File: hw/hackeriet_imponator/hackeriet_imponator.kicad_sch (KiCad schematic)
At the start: 35 parts, among them J1 USB4085-GF-A, J2 UPDI programming, J3 External Battery Connector, J4 Shitty Add On, J5 Unused pins, SW1 SW_SPDT, SW2 User configurable, SW3 User configurable, U1 ATtiny804-SS, U2 MCP2221AxSL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

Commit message: More routing
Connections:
- net ACC_ENABLE: now also U1.2 (PA4); no longer U1.4 (PA6)
- net ACC_INT: now also U1.13 (PA3); no longer U1.3 (PA5)
- net at SW3.1: now also U1.4 (PA6); no longer U1.2 (PA4)
- net at SW2.1: now also U1.3 (PA5); no longer U1.13 (PA3)
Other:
- moved on the sheet: SW2, SW3
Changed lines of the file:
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@@
 	(wire
 		(pts
-			(xy 81.28 58.42) (xy 109.22 58.42)
+			(xy 40.64 48.26) (xy 50.8 48.26)
 		)
 		(stroke
@@
 	(wire
 		(pts
-			(xy 40.64 48.26) (xy 50.8 48.26)
+			(xy 187.96 139.7) (xy 187.96 137.16)
 		)
 		(stroke
@@
 	(wire
 		(pts
-			(xy 187.96 139.7) (xy 187.96 137.16)
+			(xy 111.76 66.04) (xy 111.76 63.5)
 		)
 		(stroke
@@
 	(wire
 		(pts
-			(xy 111.76 55.88) (xy 111.76 59.69)
+			(xy 81.28 63.5) (xy 111.76 63.5)
 		)
 		(stroke
@@
 	(wire
 		(pts
-			(xy 121.92 64.77) (xy 124.46 64.77)
+			(xy 121.92 66.04) (xy 124.46 66.04)
 		)
 		(stroke
@@
 	(wire
 		(pts
-			(xy 109.22 58.42) (xy 109.22 64.77)
+			(xy 168.91 90.17) (xy 179.07 90.17)
 		)
 		(stroke
@@
 	(wire
 		(pts
-			(xy 168.91 90.17) (xy 179.07 90.17)
+			(xy 69.85 118.11) (xy 72.39 118.11)
 		)
 		(stroke
@@
 	(wire
 		(pts
-			(xy 69.85 118.11) (xy 72.39 118.11)
+			(xy 81.28 60.96) (xy 111.76 60.96)
 		)
 		(stroke
@@
 	(wire
 		(pts
-			(xy 121.92 59.69) (xy 124.46 59.69)
+			(xy 121.92 60.96) (xy 124.46 60.96)
 		)
 		(stroke
@@
 	(wire
 		(pts
-			(xy 81.28 55.88) (xy 111.76 55.88)
-		)
-		(stroke
-			(width 0)
-			(type default)
-		)
-	)
-	(wire
-		(pts
 			(xy 62.23 114.3) (xy 62.23 113.03)
 		)
@@
 	(wire
 		(pts
-			(xy 109.22 64.77) (xy 111.76 64.77)
-		)
-		(stroke
-			(width 0)
-			(type default)
-		)
-	)
-	(wire
-		(pts
 			(xy 96.52 179.07) (xy 99.06 179.07)
 		)
@@
 		)
 	)
-	(global_label "PA5"
-		(shape input)
-		(at 81.28 60.96 0)
-		(fields_autoplaced yes)
-		(effects
-			(font
-				(size 1.27 1.27)
-			)
-			(justify left)
-		)
-		(property "Intersheetrefs" "${INTERSHEET_REFS}"
-			(at 87.8333 60.96 0)
-			(effects
-				(font
-					(size 1.27 1.27)
-				)
-				(justify left)
-				(hide yes)
-			)
-		)
-	)
 	(global_label "WS2812B LED RGB Control logo"
 		(shape input)
@@
 		)
 	)
-	(global_label "PA5"
+	(global_label "PA3"
 		(shape input)
 		(at 168.91 92.71 180)
@@
 		)
 	)
-	(global_label "PA5"
+	(global_label "PA3"
 		(shape input)
 		(at 130.81 180.34 180)
@@
 		)
 	)
-	(global_label "PA6"
+	(global_label "PA4"
 		(shape input)
 		(at 130.81 182.88 180)
@@
 		)
 	)
-	(global_label "SDA"
+	(global_label "PA4"
 		(shape input)
-		(at 111.76 179.07 0)
+		(at 81.28 58.42 0)
 		(fields_autoplaced yes)
 		(effects
@@
 		)
 		(property "Intersheetrefs" "${INTERSHEET_REFS}"
-			(at 118.3133 179.07 0)
+			(at 87.8333 58.42 0)
 			(effects
 				(font
@@
 		)
 	)
-	(global_label "D-"
+	(global_label "SDA"
 		(shape input)
-		(at 78.74 128.27 180)
+		(at 111.76 179.07 0)
 		(fields_autoplaced yes)
 		(effects
@@
 				(size 1.27 1.27)
 			)
-			(justify right)
+			(justify left)
 		)
 		(property "Intersheetrefs" "${INTERSHEET_REFS}"
-			(at 72.9124 128.27 0)
+			(at 118.3133 179.07 0)
 			(effects
 				(font
 					(size 1.27 1.27)
 				)
-				(justify right)
+				(justify left)
 				(hide yes)
 			)
 		)
 	)
-	(global_label "PA6"
+	(global_label "D-"
 		(shape input)
-		(at 81.28 63.5 0)
+		(at 78.74 128.27 180)
 		(fields_autoplaced yes)
 		(effects
@@
 				(size 1.27 1.27)
 			)
-			(justify left)
+			(justify right)
 		)
 		(property "Intersheetrefs" "${INTERSHEET_REFS}"
-			(at 87.8333 63.5 0)
+			(at 72.9124 128.27 0)
 			(effects
 				(font
 					(size 1.27 1.27)
 				)
-				(justify left)
+				(justify right)
 				(hide yes)
 			)
@@
 		)
 	)
+	(global_label "PA3"
+		(shape input)
+		(at 81.28 55.88 0)
+		(fields_autoplaced yes)
+		(effects
+			(font
+				(size 1.27 1.27)
+			)
+			(justify left)
+		)
+		(property "Intersheetrefs" "${INTERSHEET_REFS}"
+			(at 87.8333 55.88 0)
+			(effects
+				(font
+					(size 1.27 1.27)
+				)
+				(justify left)
+				(hide yes)
+			)
+		)
+	)
 	(global_label "Attiny UART RX"
 		(shape input)
@@
 		)
 	)
-	(global_label "PA6"
+	(global_label "PA4"
 		(shape input)
 		(at 168.91 90.17 180)
@@
 	(symbol
 		(lib_id "power:GND")
-		(at 124.46 59.69 0)
+		(at 124.46 60.96 0)
 		(unit 1)
 		(exclude_from_sim no)
@@
 		(dnp no)
 		(property "Reference" "#PWR038"
-			(at 124.46 66.04 0)
+			(at 124.46 67.31 0)
 			(effects
 				(font
@@
 		)
 		(property "Value" "GND"
-			(at 125.476 62.738 0)
+			(at 125.476 64.008 0)
 			(effects
 				(font
@@
 		)
 		(property "Footprint" ""
-			(at 124.46 59.69 0)
+			(at 124.46 60.96 0)
 			(effects
 				(font
@@
 		)
 		(property "Datasheet" ""
-			(at 124.46 59.69 0)
+			(at 124.46 60.96 0)
 			(effects
 				(font
@@
 		)
 		(property "Description" "Power symbol creates a global label with name \"GND\" , ground"
-			(at 124.46 59.69 0)
+			(at 124.46 60.96 0)
 			(effects
 				(font
@@
 	(symbol
 		(lib_id "Switch:SW_Push")
-		(at 116.84 64.77 0)
+		(at 116.84 66.04 0)
 		(unit 1)
 		(exclude_from_sim no)
@@
 		(dnp no)
 		(property "Reference" "SW3"
-			(at 119.126 62.23 0)
+			(at 119.126 63.5 0)
 			(effects
 				(font
@@
 		)
 		(property "Value" "User configurable"
-			(at 107.442 62.23 0)
+			(at 107.442 63.5 0)
 			(effects
 				(font
@@
 		)
 		(property "Footprint" "Button_Switch_SMD:SW_SPST_EVQP7C"
-			(at 116.84 59.69 0)
+			(at 116.84 60.96 0)
 			(effects
 				(font
@@
 		)
 		(property "Datasheet" "~"
-			(at 116.84 59.69 0)
+			(at 116.84 60.96 0)
 			(effects
 				(font
@@
 		)
 		(property "Description" "Push button switch, generic, two pins"
-			(at 116.84 64.77 0)
+			(at 116.84 66.04 0)
 			(effects
 				(font
@@
 	(symbol
 		(lib_id "Switch:SW_Push")
-		(at 116.84 59.69 0)
+		(at 116.84 60.96 0)
 		(unit 1)
 		(exclude_from_sim no)
@@
 		(dnp no)
 		(property "Reference" "SW2"
-			(at 119.38 56.896 0)
+			(at 119.38 58.166 0)
 			(effects
 				(font
@@
 		)
 		(property "Value" "User configurable"
-			(at 128.016 57.658 0)
+			(at 128.016 58.928 0)
 			(effects
 				(font
@@
 		)
 		(property "Footprint" "Button_Switch_SMD:SW_SPST_EVQP7C"
-			(at 116.84 54.61 0)
+			(at 116.84 55.88 0)
 			(effects
 				(font
@@
 		)
 		(property "Datasheet" "~"
-			(at 116.84 54.61 0)
+			(at 116.84 55.88 0)
 			(effects
 				(font
@@
 		)
 		(property "Description" "Push button switch, generic, two pins"
-			(at 116.84 59.69 0)
+			(at 116.84 60.96 0)
 			(effects
 				(font
@@
 	(symbol
 		(lib_id "power:GND")
-		(at 124.46 64.77 0)
+		(at 124.46 66.04 0)
 		(unit 1)
 		(exclude_from_sim no)
@@
 		(dnp no)
 		(property "Reference" "#PWR039"
-			(at 124.46 71.12 0)
+			(at 124.46 72.39 0)
 			(effects
 				(font
@@
 		)
 		(property "Value" "GND"
-			(at 125.222 67.818 0)
+			(at 125.222 69.088 0)
 			(effects
 				(font
@@
 		)
 		(property "Footprint" ""
-			(at 124.46 64.77 0)
+			(at 124.46 66.04 0)
 			(effects
 				(font
@@
 		)
 		(property "Datasheet" ""
-			(at 124.46 64.77 0)
+			(at 124.46 66.04 0)
 			(effects
 				(font
@@
 		)
 		(property "Description" "Power symbol creates a global label with name \"GND\" , ground"
-			(at 124.46 64.77 0)
+			(at 124.46 66.04 0)
 			(effects
 				(font

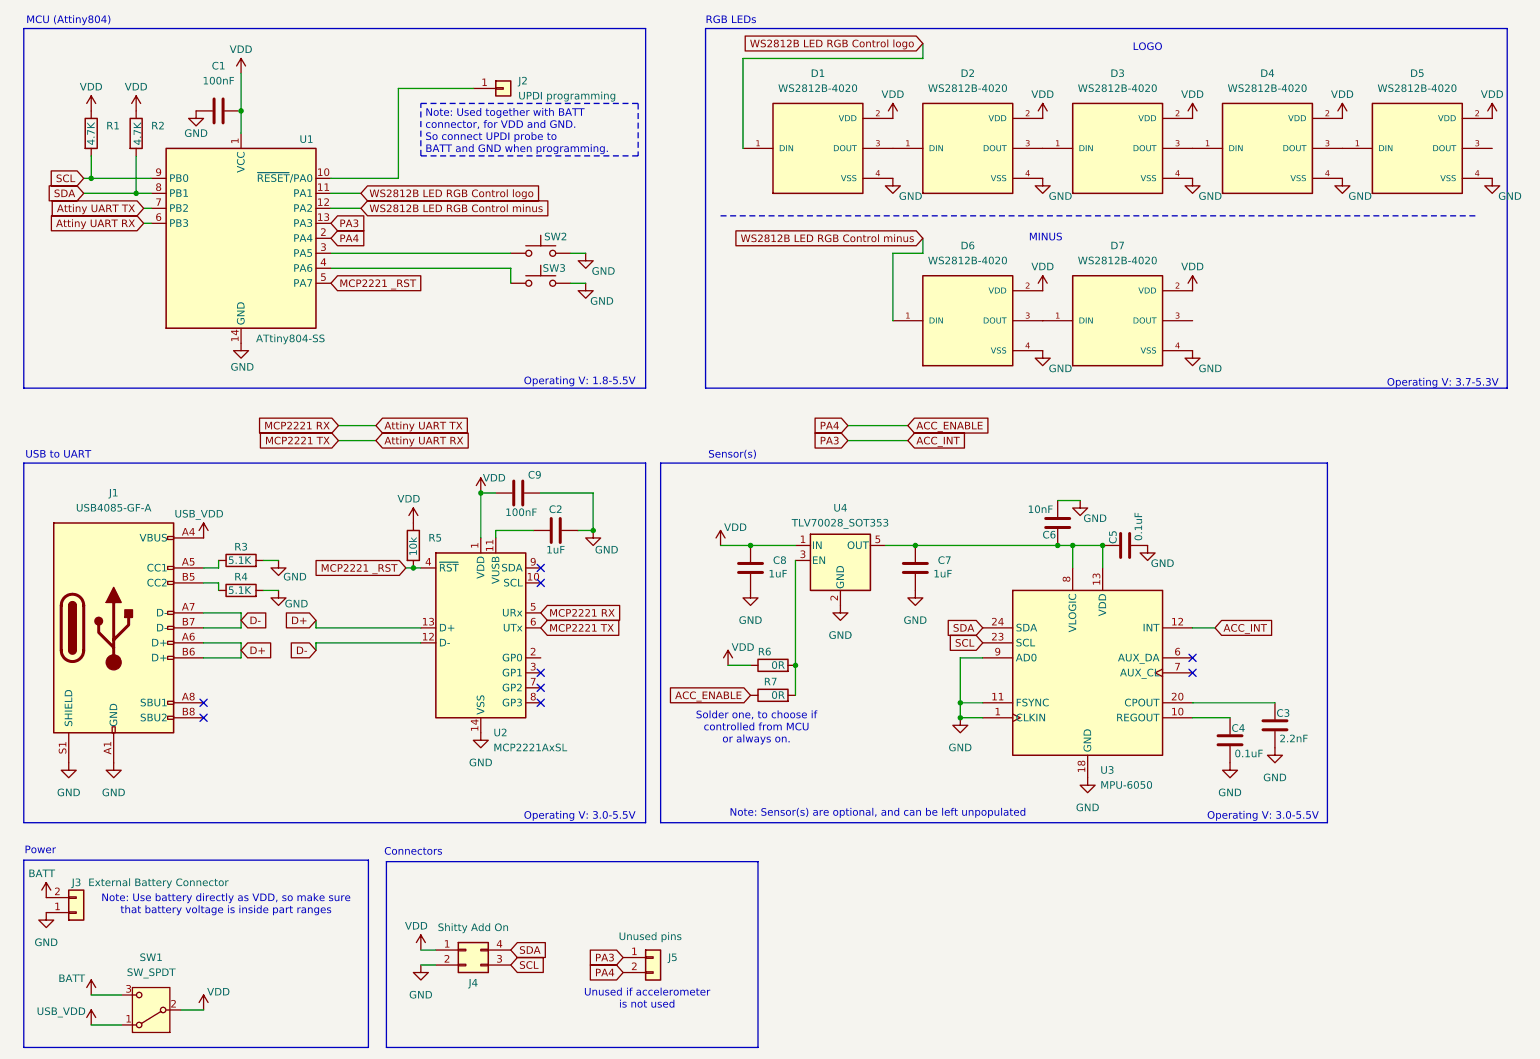
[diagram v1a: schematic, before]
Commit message: Added Logic Level Converter. Added GND vias. Routed the rest. Ran Design Rules test and fixed stuff.
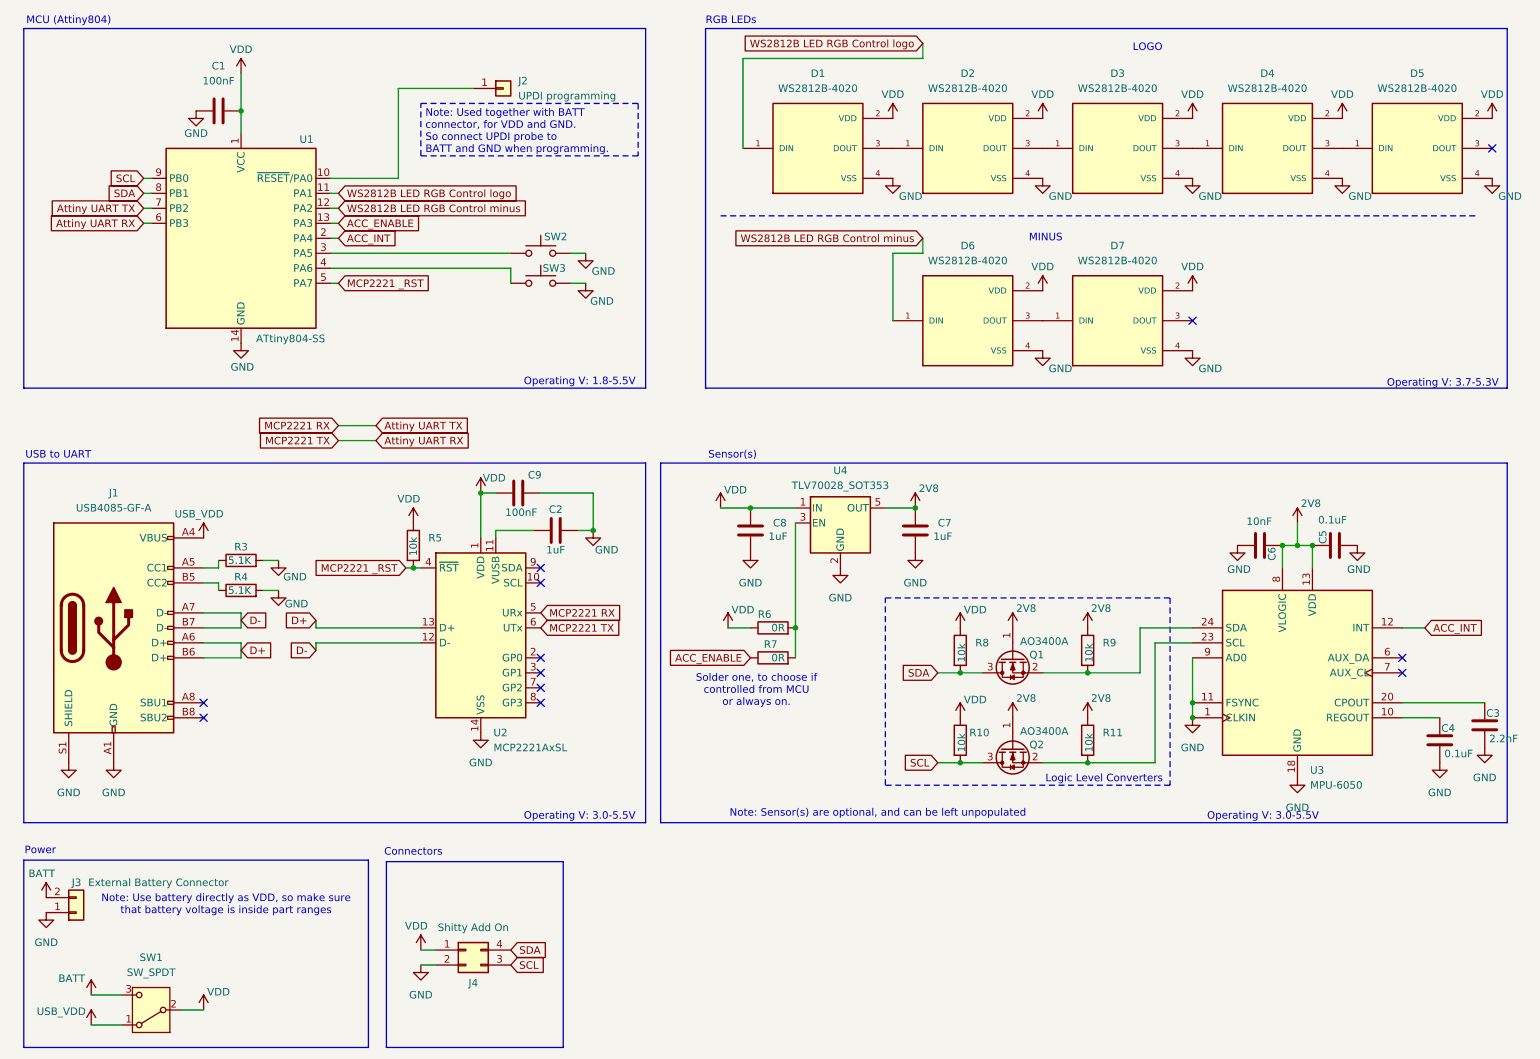
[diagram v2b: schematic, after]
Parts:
- removed J5: Unused pins, Connector_PinSocket_2.54mm:PinSocket_1x02_P2.54mm_Vertical_SMD_Pin1Right, symbol Connector_Generic:Conn_01x02
- removed R1, R2: 4.7K, Resistor_SMD:R_0603_1608Metric_Pad0.98x0.95mm_HandSolder, symbol Device:R
- added Q1, Q2: AO3400A, Package_TO_SOT_SMD:SOT-23, symbol Transistor_FET:AO3400A
- added R10, R11, R8, R9: 10k, Resistor_SMD:R_0603_1608Metric_Pad0.98x0.95mm_HandSolder, symbol Device:R
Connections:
- net ACC_ENABLE: now also U1.13 (PA3); no longer U1.2 (PA4)
- net ACC_INT: now also U1.2 (PA4); no longer U1.13 (PA3)
- net SCL: now also Q2.3 (D), R10.2; no longer U3.23 (SCL)
- net SDA: now also Q1.3 (D), R8.2; no longer U3.24 (SDA)
- net VDD: now also R10.1, R8.1
- net 2V8: now reaches C5.2, C6.2, C7.1, U3.13 (VDD), U3.8 (VLOGIC), U4.5 (OUT)
- net 2V8: now also Q1.1 (G), Q2.1 (G), R11.1, R9.1
- new net: Q1.2 (S), R9.2, U3.24 (SDA)
- new net: Q2.2 (S), R11.2, U3.23 (SCL)
- no-connect marks 9 -> 12
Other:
- note added: "Logic Level Converters"
- note removed: "Unused if accelerometer is not used"
- moved on the sheet: C3, C4, C5, C6, C7, C8, R6, R7, U3, U4
